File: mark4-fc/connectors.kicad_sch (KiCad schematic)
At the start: 5 parts, among them J3 Conn_01x04, J4 Conn_01x06, J5 Conn_01x04, J6 Conn_01x08

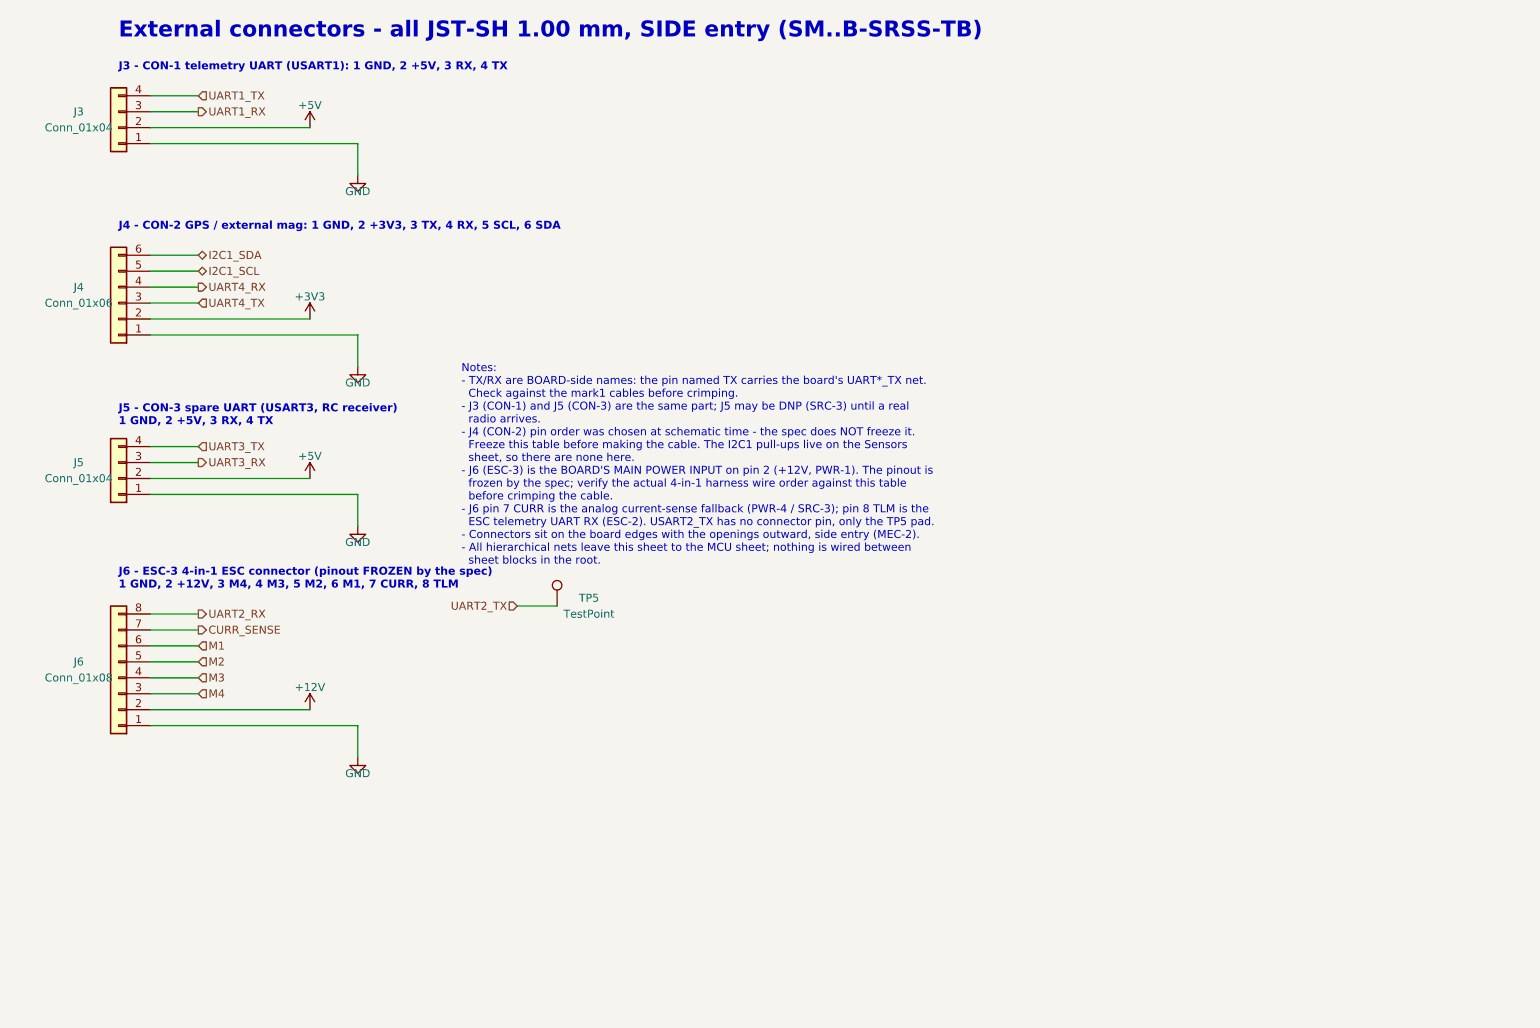
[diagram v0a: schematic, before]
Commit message: feat(hardware): shrink mark4-fc to 36x36 and split assembly by side
Board outline, connectors and assembly strategy all move in one pass;
schematic, PCB and the fab package are propagated together.

- Rebuild the Edge.Cuts outline at 36x36 (the floor the 30.5 mm M3
  pattern allows) and fix the four corner fillets whose arc midpoints
  sat diametrically opposite, which cut a 4 mm disc out of each corner.
- Reduce SWD from 6 to 3 positions (SWDIO/SWCLK/GND) so SWD plus USB-C
  fit the edge budget; SWO is gone, BOOT0 stays the recovery path.
- Move the hand-soldered parts (LDO, flash, Q1, JP1, test points and
  their pull-ups) to the bottom face; the JLCPCB package now covers the
  top side only (CPL 63 -> 52, BOM 31 -> 26 lines).
- Re-relax the placement into the smaller outline with the electrically
  critical groups hand-anchored (crystal, VCAP, buck corner, connector
  ESD); LED strip pads move to the left edge to clear the USB row.
  DRC clean, schematic parity 0, nothing routed yet.
- Hide top-silk refdes and values in favour of pad labels, add the
  orientation arrow (direction still to confirm against the frame).
- Replace the footprint-family CPL rotation table with measured,
  LCSC-keyed corrections (jlcpcb-cpl-rotations.csv), derived from the
  EasyEDA footprints; fixes U2, U1 and Q1 which the community table got
  wrong or missed.
- Correct the STO-2 flash substitution note: no 256 Mbit Winbond exists
  in SOIC-8 208 mil; list the real drop-ins and the EN4B firmware cost.

Co-Authored-By: Claude Fable 5 <noreply@anthropic.com>
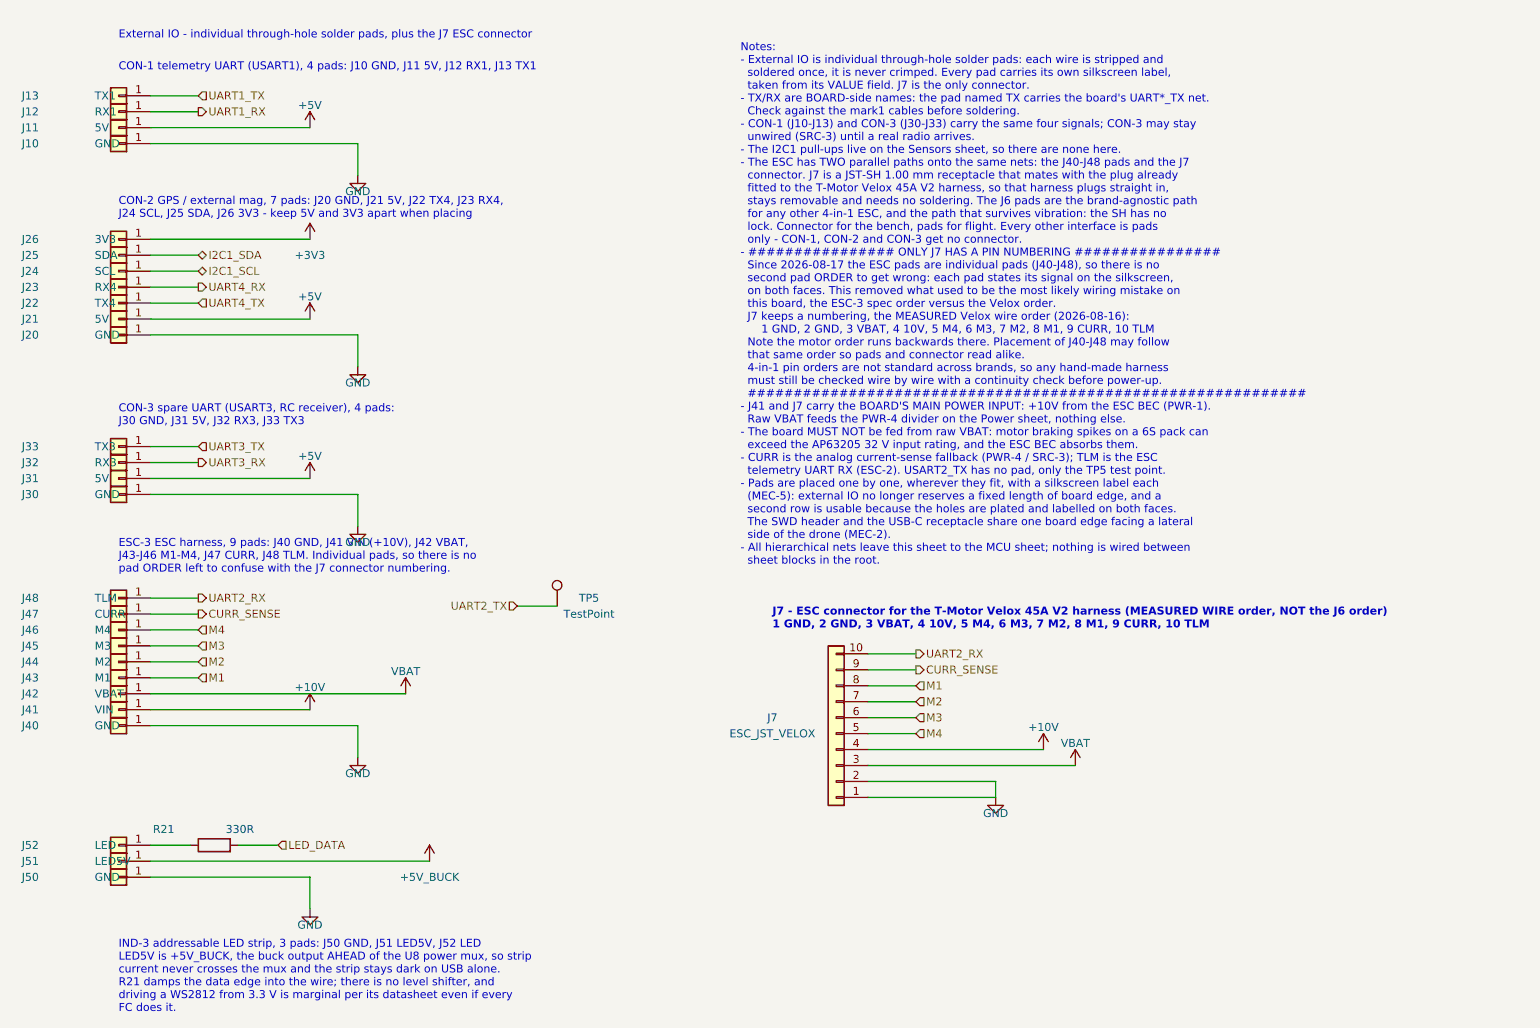
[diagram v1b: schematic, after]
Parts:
- removed J3, J5: Conn_01x04, Connector_JST:JST_SH_SM04B-SRSS-TB_1x04-1MP_P1.00mm_Horizontal, symbol Connector_Generic:Conn_01x04
- removed J4: Conn_01x06, Connector_JST:JST_SH_SM06B-SRSS-TB_1x06-1MP_P1.00mm_Horizontal, symbol Connector_Generic:Conn_01x06
- removed J6: Conn_01x08, Connector_JST:JST_SH_SM08B-SRSS-TB_1x08-1MP_P1.00mm_Horizontal, symbol Connector_Generic:Conn_01x08
- added J10, J20, J30, J40, J50: GND, mark4-fc:SolderPad_1x01_THT, symbol Connector_Generic:Conn_01x01
- added J11, J21, J31: 5V, mark4-fc:SolderPad_1x01_THT, symbol Connector_Generic:Conn_01x01
- added J12: RX1, mark4-fc:SolderPad_1x01_THT, symbol Connector_Generic:Conn_01x01
- added J13: TX1, mark4-fc:SolderPad_1x01_THT, symbol Connector_Generic:Conn_01x01
- added J22: TX4, mark4-fc:SolderPad_1x01_THT, symbol Connector_Generic:Conn_01x01
- added J23: RX4, mark4-fc:SolderPad_1x01_THT, symbol Connector_Generic:Conn_01x01
- added J24: SCL, mark4-fc:SolderPad_1x01_THT, symbol Connector_Generic:Conn_01x01
- added J25: SDA, mark4-fc:SolderPad_1x01_THT, symbol Connector_Generic:Conn_01x01
- added J26: 3V3, mark4-fc:SolderPad_1x01_THT, symbol Connector_Generic:Conn_01x01
- added J32: RX3, mark4-fc:SolderPad_1x01_THT, symbol Connector_Generic:Conn_01x01
- added J33: TX3, mark4-fc:SolderPad_1x01_THT, symbol Connector_Generic:Conn_01x01
- added J41: VIN, mark4-fc:SolderPad_1x01_THT, symbol Connector_Generic:Conn_01x01
- added J42: VBAT, mark4-fc:SolderPad_1x01_THT, symbol Connector_Generic:Conn_01x01
- added J43: M1, mark4-fc:SolderPad_1x01_THT, symbol Connector_Generic:Conn_01x01
- added J44: M2, mark4-fc:SolderPad_1x01_THT, symbol Connector_Generic:Conn_01x01
- added J45: M3, mark4-fc:SolderPad_1x01_THT, symbol Connector_Generic:Conn_01x01
- added J46: M4, mark4-fc:SolderPad_1x01_THT, symbol Connector_Generic:Conn_01x01
- added J47: CURR, mark4-fc:SolderPad_1x01_THT, symbol Connector_Generic:Conn_01x01
- added J48: TLM, mark4-fc:SolderPad_1x01_THT, symbol Connector_Generic:Conn_01x01
- added J51: LED5V, mark4-fc:SolderPad_1x01_THT, symbol Connector_Generic:Conn_01x01
- added J52: LED, mark4-fc:SolderPad_1x01_THT, symbol Connector_Generic:Conn_01x01
- added J7: ESC_JST_VELOX, Connector_JST:JST_SH_SM10B-SRSS-TB_1x10-1MP_P1.00mm_Horizontal, symbol Connector_Generic:Conn_01x10
- added R21: 330R, Resistor_SMD:R_0603_1608Metric, symbol Device:R
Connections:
- net +3V3: now also J26.1 (Pin_1)
- net +5V: now also J11.1 (Pin_1), J21.1 (Pin_1), J31.1 (Pin_1)
- net CURR_SENSE: now also J47.1 (Pin_1), J7.9 (Pin_9)
- net GND: now also J10.1 (Pin_1), J20.1 (Pin_1), J30.1 (Pin_1), J40.1 (Pin_1), J50.1 (Pin_1), J7.1 (Pin_1), J7.2 (Pin_2)
- net I2C1_SCL: now also J24.1 (Pin_1)
- net I2C1_SDA: now also J25.1 (Pin_1)
- net M1: now also J43.1 (Pin_1), J7.8 (Pin_8)
- net M2: now also J44.1 (Pin_1), J7.7 (Pin_7)
- net M3: now also J45.1 (Pin_1), J7.6 (Pin_6)
- net M4: now also J46.1 (Pin_1), J7.5 (Pin_5)
- net UART1_RX: now also J12.1 (Pin_1)
- net UART1_TX: now also J13.1 (Pin_1)
- net UART2_RX: now also J48.1 (Pin_1), J7.10 (Pin_10)
- net UART3_RX: now also J32.1 (Pin_1)
- net UART3_TX: now also J33.1 (Pin_1)
- net UART4_RX: now also J23.1 (Pin_1)
- net UART4_TX: now also J22.1 (Pin_1)
- new net: J52.1 (Pin_1), R21.1
- new net +10V: J41.1 (Pin_1), J7.4 (Pin_4)
- new net +5V_BUCK: J51.1 (Pin_1)
- new net LED_DATA: R21.2
- new net VBAT: J42.1 (Pin_1), J7.3 (Pin_3)
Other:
- note added: "CON-1 telemetry UART (USART1), 4 pads: J10 GND, J11 5V, J12 RX1, J13 TX1"
- note added: "CON-2 GPS / external mag, 7 pads: J20 GND, J21 5V, J22 TX4, J23 RX4, J24 SCL, J25 SDA, J26 3V3 - keep 5V and 3V3 apart when placing"
- note added: "CON-3 spare UART (USART3, RC receiver), 4 pads: J30 GND, J31 5V, J32 RX3, J33 TX3"
- note added: "ESC-3 ESC harness, 9 pads: J40 GND, J41 VIN (+10V), J42 VBAT, J43-J46 M1-M4, J47 CURR, J48 TLM. Individual pads, so there is no pad ORDER left to confuse with the J7 connector numbering."
- note added: "External IO - individual through-hole solder pads, plus the J7 ESC connector"
- note added: "IND-3 addressable LED strip, 3 pads: J50 GND, J51 LED5V, J52 LED LED5V is +5V_BUCK, the buck output AHEAD of the U8 power mux, so strip current never crosses the mux and the strip stays dark on USB alone. R21 damps the data edge into the wire; there is no level shifter, and driving a WS2812 from 3.3 V is marginal per its datasheet even if every FC does it."
- note added: "J7 - ESC connector for the T-Motor Velox 45A V2 harness (MEASURED WIRE order, NOT the J6 order) 1 GND, 2 GND, 3 VBAT, 4 10V, 5 M4, 6 M3, 7 M2, 8 M1, 9 CURR, 10 TLM"
- note added: "Notes: - External IO is individual through-hole solder pads: each wire is stripped and soldered once, it is never crimped. Every pad carries its own silkscreen label, taken from its VALUE field. J7 is the only connector. - TX/RX are BOARD-side names: the pad named TX carries the board's UART*_TX net. Check against the mark1 cables before soldering. - CON-1 (J10-J13) and CON-3 (J30-J33) carry the 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"
- note removed: "External connectors - all JST-SH 1.00 mm, SIDE entry (SM..B-SRSS-TB)"
- note removed: "J3 - CON-1 telemetry UART (USART1): 1 GND, 2 +5V, 3 RX, 4 TX"
- note removed: "J4 - CON-2 GPS / external mag: 1 GND, 2 +3V3, 3 TX, 4 RX, 5 SCL, 6 SDA"
- note removed: "J5 - CON-3 spare UART (USART3, RC receiver) 1 GND, 2 +5V, 3 RX, 4 TX"
- note removed: "J6 - ESC-3 4-in-1 ESC connector (pinout FROZEN by the spec) 1 GND, 2 +12V, 3 M4, 4 M3, 5 M2, 6 M1, 7 CURR, 8 TLM"
- note removed: "Notes: - TX/RX are BOARD-side names: the pin named TX carries the board's UART*_TX net. Check against the mark1 cables before crimping. - J3 (CON-1) and J5 (CON-3) are the same part; J5 may be DNP (SRC-3) until a real radio arrives. - J4 (CON-2) pin order was chosen at schematic time - the spec does NOT freeze it. Freeze this table before making the cable. The I2C1 pull-ups live on the Sensors sh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"
